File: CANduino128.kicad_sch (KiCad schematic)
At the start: 63 parts, among them J1 Conn_02x32_Row_Letter_First, J2 Conn_01x10, U1 AVR-H128-CAN, U2 74AHC373

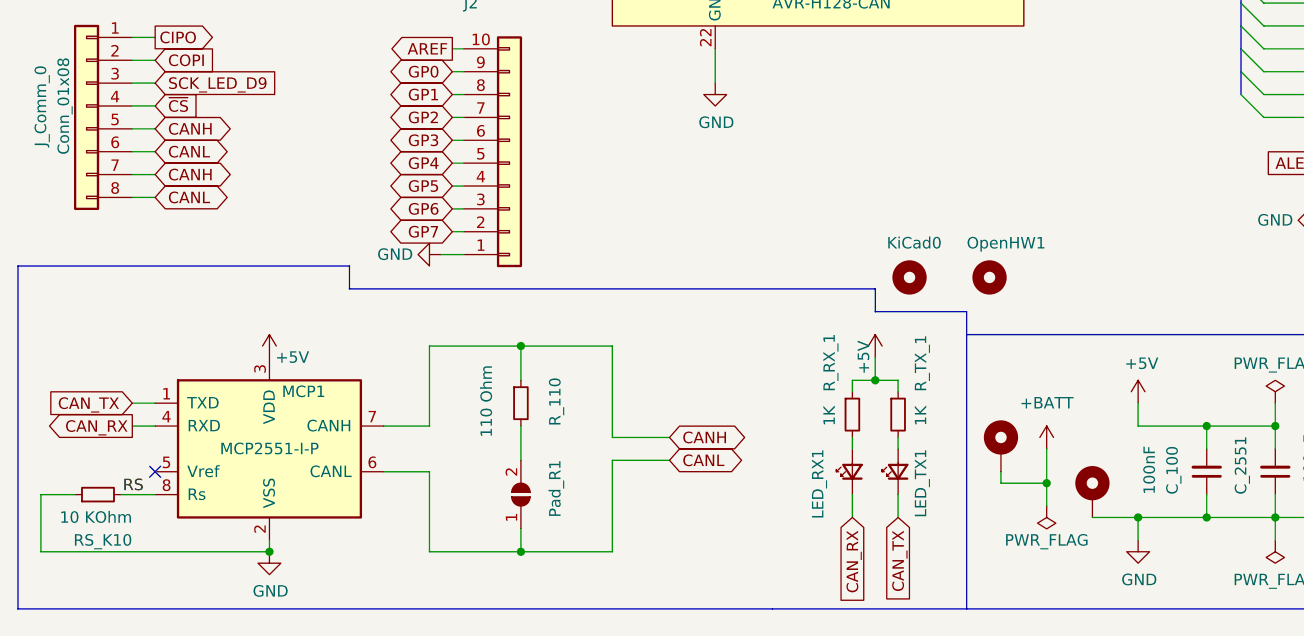
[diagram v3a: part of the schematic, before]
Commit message: Adieu le connecteur sous l'AT90CAN128
git-svn-id: file:///D%5C00%20-%20Dev%20&%20Calculs%5CRepoTortoiseSVN_PCB%5CCANduino128/tags/CANduino128%20-%20v3.0@75 67ddf66f-3787-a644-8df7-7746e21a92b3
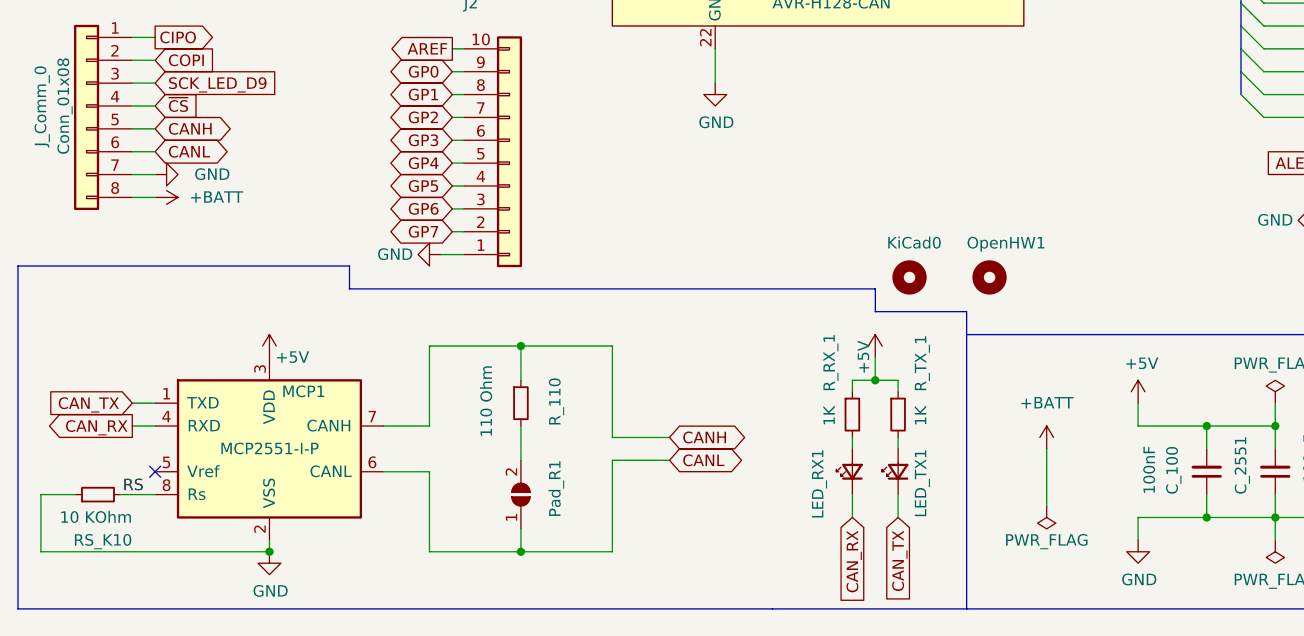
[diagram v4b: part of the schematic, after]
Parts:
- removed H5, H6: MountingHole_Pad, Connector_Wire:SolderWire-0.1sqmm_1x01_D0.4mm_OD1mm_Relief2x, symbol Mechanical:MountingHole_Pad
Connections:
- net +BATT: now also J_Comm_0.8 (Pin_8)
- net CANH: no longer J_Comm_0.7 (Pin_7)
- net CANL: no longer J_Comm_0.8 (Pin_8)
- net GND: now also J_Comm_0.7 (Pin_7)
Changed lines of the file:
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@@
   (junction (at 60.96 116.84) (diameter 0) (color 0 0 0 0)
   )
-  (junction (at 138.43 186.69) (diameter 0) (color 0 0 0 0)
-  )
   (junction (at 251.46 41.91) (diameter 0) (color 0 0 0 0)
   )
@@
   (junction (at 41.91 190.5) (diameter 0) (color 0 0 0 0)
   )
-  (junction (at 128.27 182.88) (diameter 0) (color 0 0 0 0)
-  )
   (junction (at 189.23 64.77) (diameter 0) (color 0 0 0 0)
   )
@@
     (stroke (width 0) (type default) (color 0 0 0 0))
   )
-  (wire (pts (xy 133.35 186.69) (xy 138.43 186.69))
-    (stroke (width 0) (type default) (color 0 0 0 0))
-  )
   (wire (pts (xy 270.51 50.8) (xy 270.51 52.07))
     (stroke (width 0) (type default) (color 0 0 0 0))
@@
     (stroke (width 0) (type default) (color 0 0 0 0))
   )
-  (wire (pts (xy 123.19 181.61) (xy 123.19 182.88))
-    (stroke (width 0) (type default) (color 0 0 0 0))
-  )
   (wire (pts (xy 270.51 19.05) (xy 270.51 22.86))
     (stroke (width 0) (type default) (color 0 0 0 0))
@@
     (stroke (width 0) (type default) (color 0 0 0 0))
   )
-  (wire (pts (xy 128.27 179.07) (xy 128.27 182.88))
-    (stroke (width 0) (type default) (color 0 0 0 0))
-  )
   (wire (pts (xy 252.73 82.55) (xy 256.54 82.55))
     (stroke (width 0) (type default) (color 0 0 0 0))
@@
     (stroke (width 0) (type default) (color 0 0 0 0))
   )
-  (wire (pts (xy 123.19 182.88) (xy 128.27 182.88))
-    (stroke (width 0) (type default) (color 0 0 0 0))
-  )
   (wire (pts (xy 80.01 167.64) (xy 80.01 177.8))
     (stroke (width 0) (type default) (color 0 0 0 0))
@@
     (stroke (width 0) (type default) (color 0 0 0 0))
   )
-  (wire (pts (xy 128.27 182.88) (xy 128.27 185.42))
+  (wire (pts (xy 128.27 179.07) (xy 128.27 185.42))
     (stroke (width 0) (type default) (color 0 0 0 0))
   )
@@
     )
   )
-  (global_label "CANL" (shape bidirectional) (at 29.21 151.13 0) (fields_autoplaced)
-    (effects (font (size 1.27 1.27)) (justify left))
-    (property "Intersheet References" "${INTERSHEET_REFS}" (id 0) (at 36.3402 151.0506 0)
-      (effects (font (size 1.27 1.27)) (justify left) hide)
-    )
-  )
   (global_label "SCK_LED_D9" (shape output) (at 74.93 63.5 180) (fields_autoplaced)
     (effects (font (size 1.27 1.27)) (justify right))
@@
     )
   )
-  (global_label "CANH" (shape bidirectional) (at 29.21 148.59 0) (fields_autoplaced)
-    (effects (font (size 1.27 1.27)) (justify left))
-    (property "Intersheet References" "${INTERSHEET_REFS}" (id 0) (at 36.6426 148.5106 0)
-      (effects (font (size 1.27 1.27)) (justify left) hide)
-    )
-  )
   (global_label "ALE-D36" (shape input) (at 162.56 147.32 180) (fields_autoplaced)
     (effects (font (size 1.27 1.27)) (justify right))
@@
     (pin "1")
   )
-  (symbol (lib_id "Mechanical:MountingHole_Pad") (at 133.35 184.15 0) (unit 1)
-    (in_bom yes) (on_board yes) (fields_autoplaced)
-    (property "Reference" "H6" (id 0) (at 130.81 184.1501 0)
-      (effects (font (size 1.27 1.27)) (justify right) hide)
-    )
-    (property "Value" "MountingHole_Pad" (id 1) (at 130.81 181.6101 0)
-      (effects (font (size 1.27 1.27)) (justify right) hide)
-    )
-    (property "Footprint" "Connector_Wire:SolderWire-0.1sqmm_1x01_D0.4mm_OD1mm_Relief2x" (id 2) (at 133.35 184.15 0)
-      (effects (font (size 1.27 1.27)) hide)
-    )
-    (property "Datasheet" "~" (id 3) (at 133.35 184.15 0)
-      (effects (font (size 1.27 1.27)) hide)
-    )
-    (pin "1")
-  )
   (symbol (lib_id "Mechanical:MountingHole_Pad") (at 58.42 116.84 90) (unit 1)
     (in_bom yes) (on_board yes)
@@
     (pin "2")
   )
+  (symbol (lib_id "power:GND") (at 29.21 148.59 90) (unit 1)
+    (in_bom yes) (on_board yes)
+    (property "Reference" "#PWR?" (id 0) (at 35.56 148.59 0)
+      (effects (font (size 1.27 1.27)) hide)
+    )
+    (property "Value" "GND" (id 1) (at 35.56 148.59 90))
+    (property "Footprint" "" (id 2) (at 29.21 148.59 0)
+      (effects (font (size 1.27 1.27)) hide)
+    )
+    (property "Datasheet" "" (id 3) (at 29.21 148.59 0)
+      (effects (font (size 1.27 1.27)) hide)
+    )
+    (pin "1")
+  )
   (symbol (lib_id "Device:R_Small") (at 22.86 184.15 90) (unit 1)
     (in_bom yes) (on_board yes)
@@
     (pin "1")
   )
+  (symbol (lib_id "power:+BATT") (at 29.21 151.13 270) (unit 1)
+    (in_bom yes) (on_board yes) (fields_autoplaced)
+    (property "Reference" "#PWR?" (id 0) (at 25.4 151.13 0)
+      (effects (font (size 1.27 1.27)) hide)
+    )
+    (property "Value" "+BATT" (id 1) (at 33.02 151.1299 90)
+      (effects (font (size 1.27 1.27)) (justify left))
+    )
+    (property "Footprint" "" (id 2) (at 29.21 151.13 0)
+      (effects (font (size 1.27 1.27)) hide)
+    )
+    (property "Datasheet" "" (id 3) (at 29.21 151.13 0)
+      (effects (font (size 1.27 1.27)) hide)
+    )
+    (pin "1")
+  )
   (symbol (lib_id "Device:C_Small") (at 146.05 181.61 180) (unit 1)
     (in_bom yes) (on_board yes)
@@
     (pin "6")
   )
-  (symbol (lib_id "Mechanical:MountingHole_Pad") (at 123.19 179.07 0) (unit 1)
-    (in_bom yes) (on_board yes) (fields_autoplaced)
-    (property "Reference" "H5" (id 0) (at 125.73 176.5299 0)
-      (effects (font (size 1.27 1.27)) (justify left) hide)
-    )
-    (property "Value" "MountingHole_Pad" (id 1) (at 125.73 179.0699 0)
-      (effects (font (size 1.27 1.27)) (justify left) hide)
-    )
-    (property "Footprint" "Connector_Wire:SolderWire-0.1sqmm_1x01_D0.4mm_OD1mm_Relief2x" (id 2) (at 123.19 179.07 0)
-      (effects (font (size 1.27 1.27)) hide)
-    )
-    (property "Datasheet" "~" (id 3) (at 123.19 179.07 0)
-      (effects (font (size 1.27 1.27)) hide)
-    )
-    (pin "1")
-  )
   (symbol (lib_id "Device:LED_Small") (at 27.94 31.75 0) (unit 1)
     (in_bom yes) (on_board yes)
@@
       (reference "#PWR0147") (unit 1) (value "+5V") (footprint "")
     )
+    (path "/0dfabcc5-eb63-44a2-a4ad-269b8171fa55"
+      (reference "#PWR?") (unit 1) (value "GND") (footprint "")
+    )
+    (path "/17d452e7-33c5-40f6-898f-8af05cd1e67c"
+      (reference "#PWR?") (unit 1) (value "+BATT") (footprint "")
+    )
     (path "/79aedb82-5897-478d-abbc-4679fbc14d36"
       (reference "#PWR?") (unit 1) (value "+BATT") (footprint "")
@@
       (reference "H4") (unit 1) (value "MountingHole_Pad") (footprint "MountingHole:MountingHole_3.2mm_M3_DIN965_Pad")
     )
-    (path "/cbf24f51-cf83-4695-9980-57d060cf3af2"
-      (reference "H5") (unit 1) (value "MountingHole_Pad") (footprint "Connector_Wire:SolderWire-0.1sqmm_1x01_D0.4mm_OD1mm_Relief2x")
-    )
-    (path "/03da69e5-3600-4722-bd9b-a29881b9dfb7"
-      (reference "H6") (unit 1) (value "MountingHole_Pad") (footprint "Connector_Wire:SolderWire-0.1sqmm_1x01_D0.4mm_OD1mm_Relief2x")
-    )
     (path "/55d1fe45-db04-40c6-8e7e-ea4ebcaa72cf"

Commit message: git-svn-id: file:///D%5C00%20-%20Dev%20&%20Calculs%5CRepoTortoiseSVN_PCB%5CCANduino128/branches/CANduino128%20-%20v3.x@77 67ddf66f-3787-a644-8df7-7746e21a92b3
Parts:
- removed CA1, CA2, CA3, CA4, CA5, CA6, CA7, CA8: 1000pF, Capacitor_SMD:C_1210_3225Metric_Pad1.33x2.70mm_HandSolder, symbol Device:C_Small
- removed JPA1, JPA2, JPA3, JPA4, JPA5, JPA6, JPA7, JPA8: SolderJumper_2_Open, Jumper:SolderJumper-2_P1.3mm_Open_TrianglePad1.0x1.5mm, symbol Jumper:SolderJumper_2_Open
- removed R1_A1, R1_A2, R1_A3, R1_A4, R1_A5, R1_A6, R1_A7, R1_A8: 1K, Resistor_SMD:R_1210_3225Metric_Pad1.30x2.65mm_HandSolder, symbol Device:R_Small
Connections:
- net GND: no longer J1.a12 (Pin_a12), J1.a13 (Pin_a13), J1.a14 (Pin_a14), J1.a15 (Pin_a15)
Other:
- added sheet ADC_Line (ADC_Line.kicad_sch)
- added sheet ADC_Line1 (ADC_Line.kicad_sch)
- added sheet ADC_Line2 (ADC_Line.kicad_sch)
- added sheet ADC_Line3 (ADC_Line.kicad_sch)
- added sheet ADC_Line4 (ADC_Line.kicad_sch)
- added sheet ADC_Line5 (ADC_Line.kicad_sch)
- added sheet ADC_Line6 (ADC_Line.kicad_sch)
- added sheet ADC_Line7 (ADC_Line.kicad_sch)

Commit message: git-svn-id: file:///D%5C00%20-%20Dev%20&%20Calculs%5CRepoTortoiseSVN_PCB%5CCANduino128/branches/CANduino128%20-%20v3.x@78 67ddf66f-3787-a644-8df7-7746e21a92b3
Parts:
- removed J1: Conn_02x32_Row_Letter_First, AVR_H128-CAN:DIN41612_B_2x32_Female_Vertical_THT, symbol Connector_Generic:Conn_02x32_Row_Letter_First
- added BusISA8: Bus_ISA_8bit, Conn_ISA_8bits:PinSocket_2x32_P2.54mm_Vertical_TopBottom, symbol Conn_ISA_8bits:Bus_ISA_8bit
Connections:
- net +5V: now also BusISA8.29 (+5V), BusISA8.3 (+5V)
- net +BATT: now also BusISA8.9 (+12V)
- net ADR0: now also BusISA8.63 (BA00)
- net ADR0-D0: now also BusISA8.41 (DB0)
- net ADR1: now also BusISA8.62 (BA01)
- net ADR1-D1: now also BusISA8.40 (DB1)
- net ADR10: now also BusISA8.53 (BA10)
- net ADR11: now also BusISA8.52 (BA11)
- net ADR12: now also BusISA8.51 (BA12)
- net ADR13: now also BusISA8.50 (BA13)
- net ADR14: now also BusISA8.49 (BA14)
- net ADR15: now also BusISA8.48 (BA15)
- net ADR2: now also BusISA8.61 (BA02)
- net ADR2-D2: now also BusISA8.39 (DB2)
- net ADR3: now also BusISA8.60 (BA03)
- net ADR3-D3: now also BusISA8.38 (DB3)
- net ADR4: now also BusISA8.59 (BA04)
- net ADR4-D4: now also BusISA8.37 (DB4)
- net ADR5: now also BusISA8.58 (BA05)
- net ADR5-D5: now also BusISA8.36 (DB5)
- net ADR6: now also BusISA8.57 (BA06)
- net ADR6-D6: now also BusISA8.35 (DB6)
- net ADR7: now also BusISA8.56 (BA07)
- net ADR7-D7: now also BusISA8.34 (DB7)
- net ADR8: now also BusISA8.55 (BA08)
- net ADR9: now also BusISA8.54 (BA09)
- net ALE-D36: now also BusISA8.28 (BALE)
- net GND: now also BusISA8.1 (GND), BusISA8.31 (GND), BusISA8.32 (GND), BusISA8.64 (GND)
- net ICP1: now also BusISA8.20 (BCLK)
- net T0_OC0x: now also BusISA8.30 (OSC)
- net ~{RD}-D27: now also BusISA8.12 (~{SMEMR})
- net ~{RESET}: now also BusISA8.2 (RESET)
- net ~{WR}-D26: now also BusISA8.11 (~{SMEMW})
- no-connect marks 6 -> 30
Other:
- moved on the sheet: J2, J_Comm_0
